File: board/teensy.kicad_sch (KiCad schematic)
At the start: 3 parts, among them J1 RJ45_LED_Shielded, U5 Teensy4.1_DEV-16771

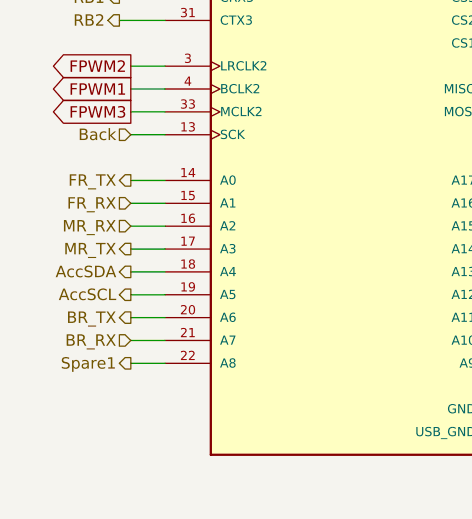
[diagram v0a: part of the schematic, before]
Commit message: Added Temp Sensor
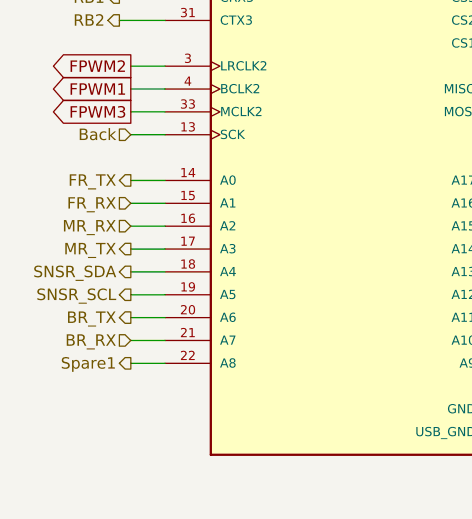
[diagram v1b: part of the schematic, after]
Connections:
- net AccSCL renamed SNSR_SCL
- net AccSDA renamed SNSR_SDA
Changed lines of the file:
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@@
 		)
 	)
-	(hierarchical_label "AccSDA"
+	(hierarchical_label "SNSR_SDA"
 		(shape output)
 		(at 71.12 134.62 180)
@@
 		)
 	)
-	(hierarchical_label "AccSCL"
+	(hierarchical_label "SNSR_SCL"
 		(shape output)
 		(at 71.12 137.16 180)

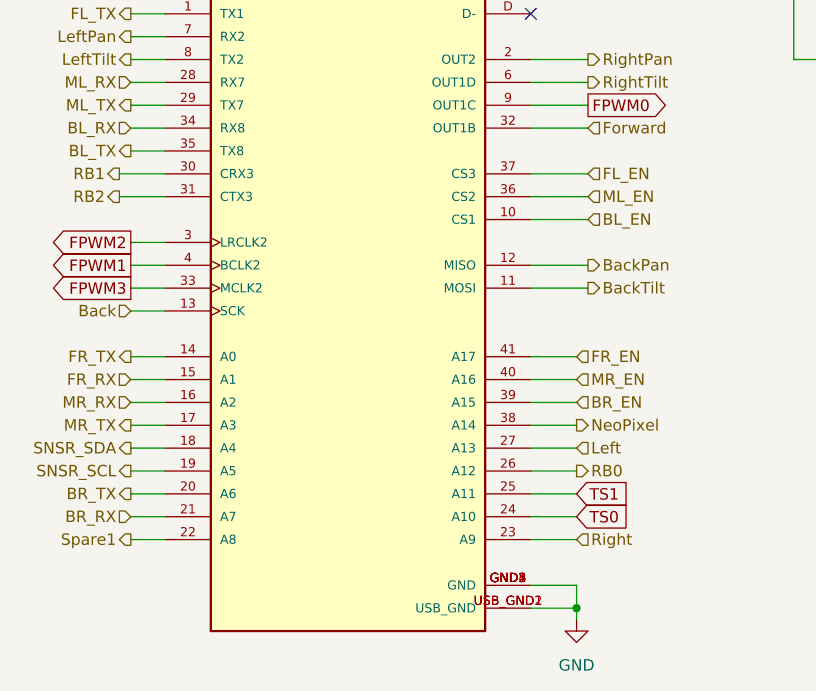
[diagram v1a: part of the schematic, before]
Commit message: Added Rotary Encoder
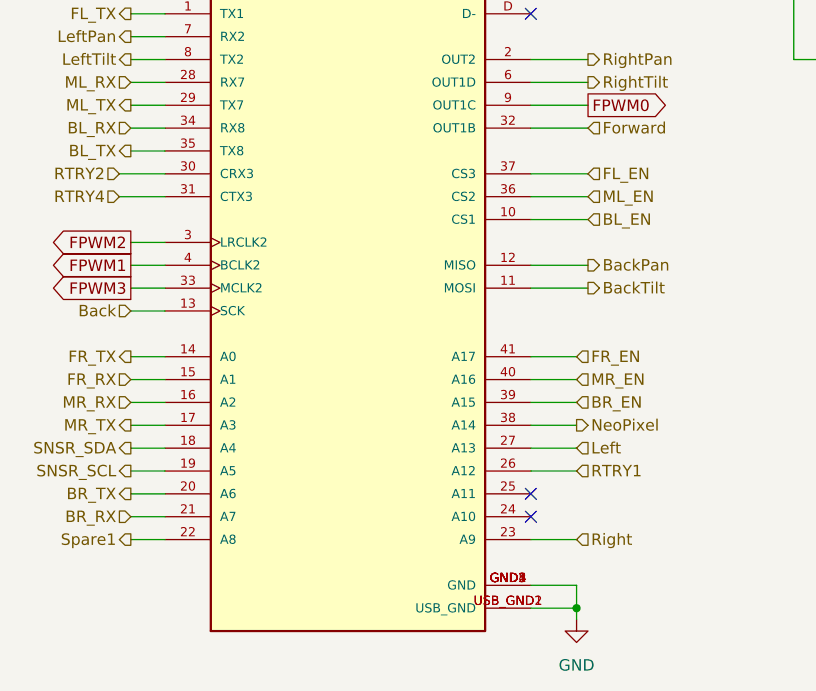
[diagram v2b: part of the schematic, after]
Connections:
- net RB0 renamed RTRY1
- net RB1 renamed RTRY2
- net RB2 renamed RTRY4
- net TS0: no longer names the net of U5.24 (A10)
- net TS1: no longer names the net of U5.25 (A11)
- no-connect marks 9 -> 11

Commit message: Fan, Light, Buck
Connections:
- net FPWM0 is gone; now on net FPWM2: U5.9 (OUT1C)
- net FPWM3 is gone; now on net FPWM1: U5.33 (MCLK2)
- net FPWM1: no longer U5.4 (BCLK2)
- net FPWM2: no longer U5.3 (LRCLK2)
- new net FTACH1: U5.3 (LRCLK2)
- new net FTACH2: U5.4 (BCLK2)

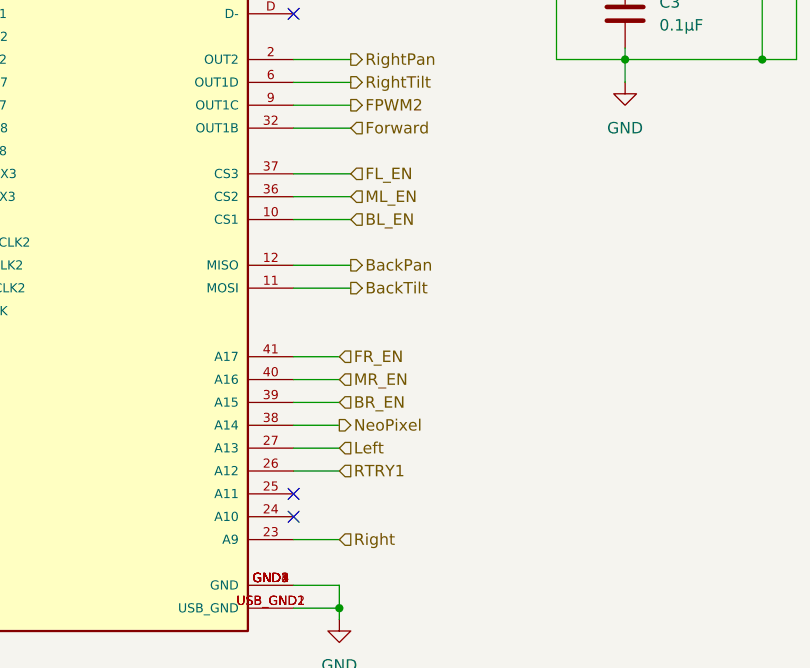
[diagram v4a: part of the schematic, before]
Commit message: routed core board
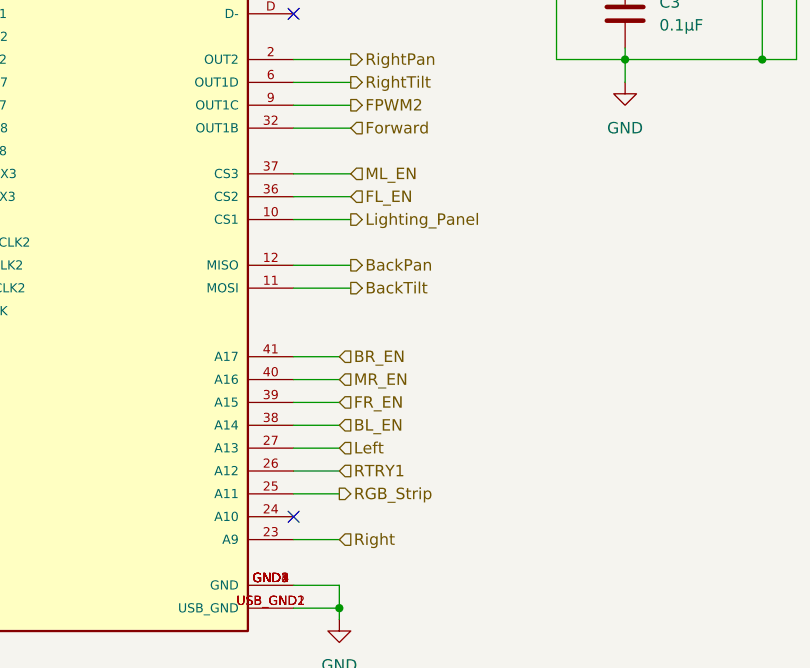
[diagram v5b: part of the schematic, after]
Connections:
- net NeoPixel is gone; now on net BL_EN: U5.38 (A14)
- net BL_EN: no longer U5.10 (CS1)
- net BR_EN: now also U5.41 (A17); no longer U5.39 (A15)
- net FL_EN: now also U5.36 (CS2); no longer U5.37 (CS3)
- net FR_EN: now also U5.39 (A15); no longer U5.41 (A17)
- net ML_EN: now also U5.37 (CS3); no longer U5.36 (CS2)
- net RGB_Strip: now reaches U5.25 (A11)
- new net Lighting_Panel: U5.10 (CS1)
- no-connect marks 11 -> 10

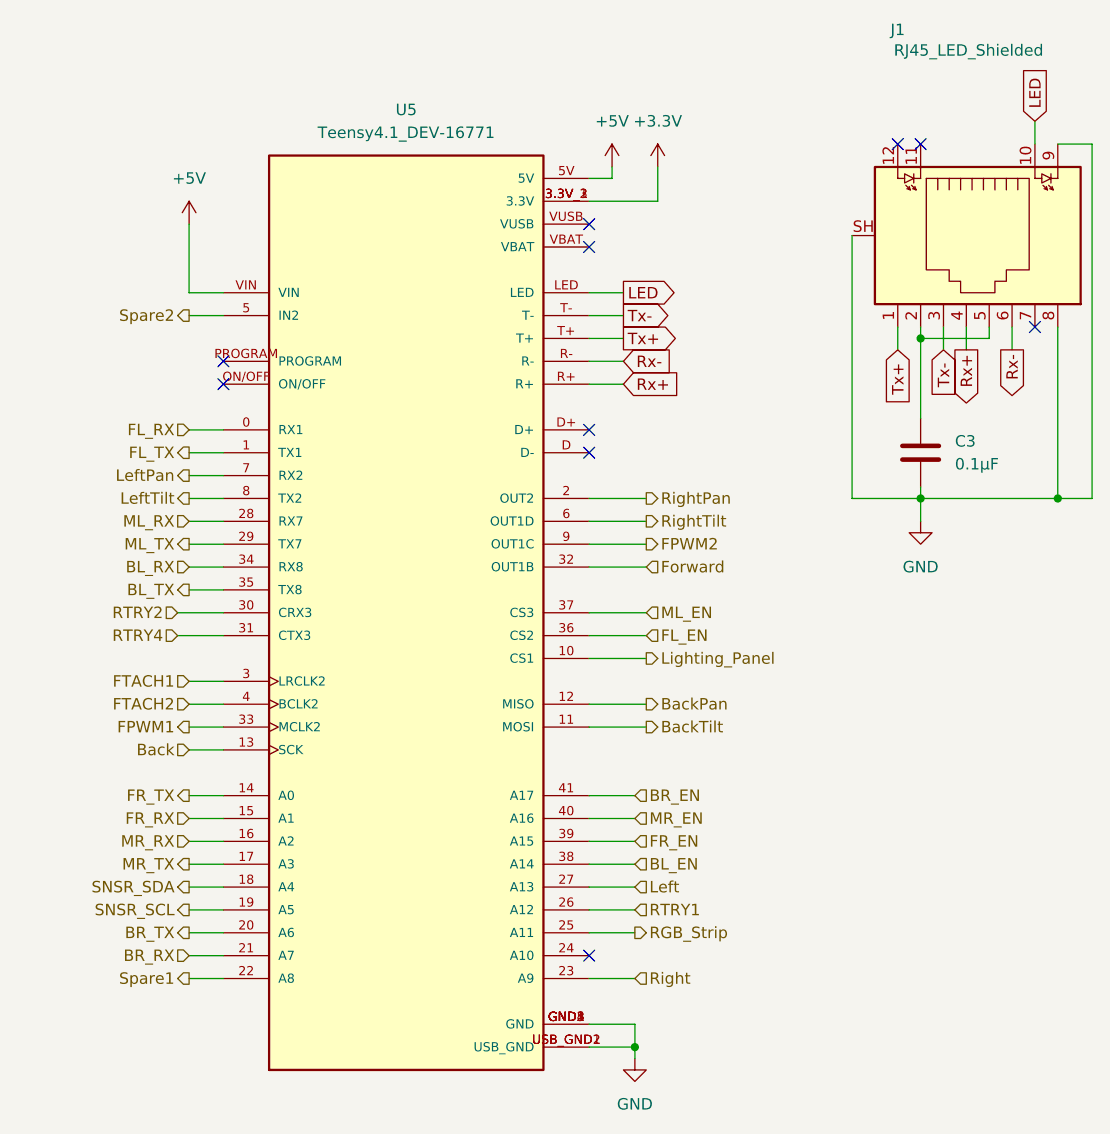
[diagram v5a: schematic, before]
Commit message: Cleaned up traces and silkscreens
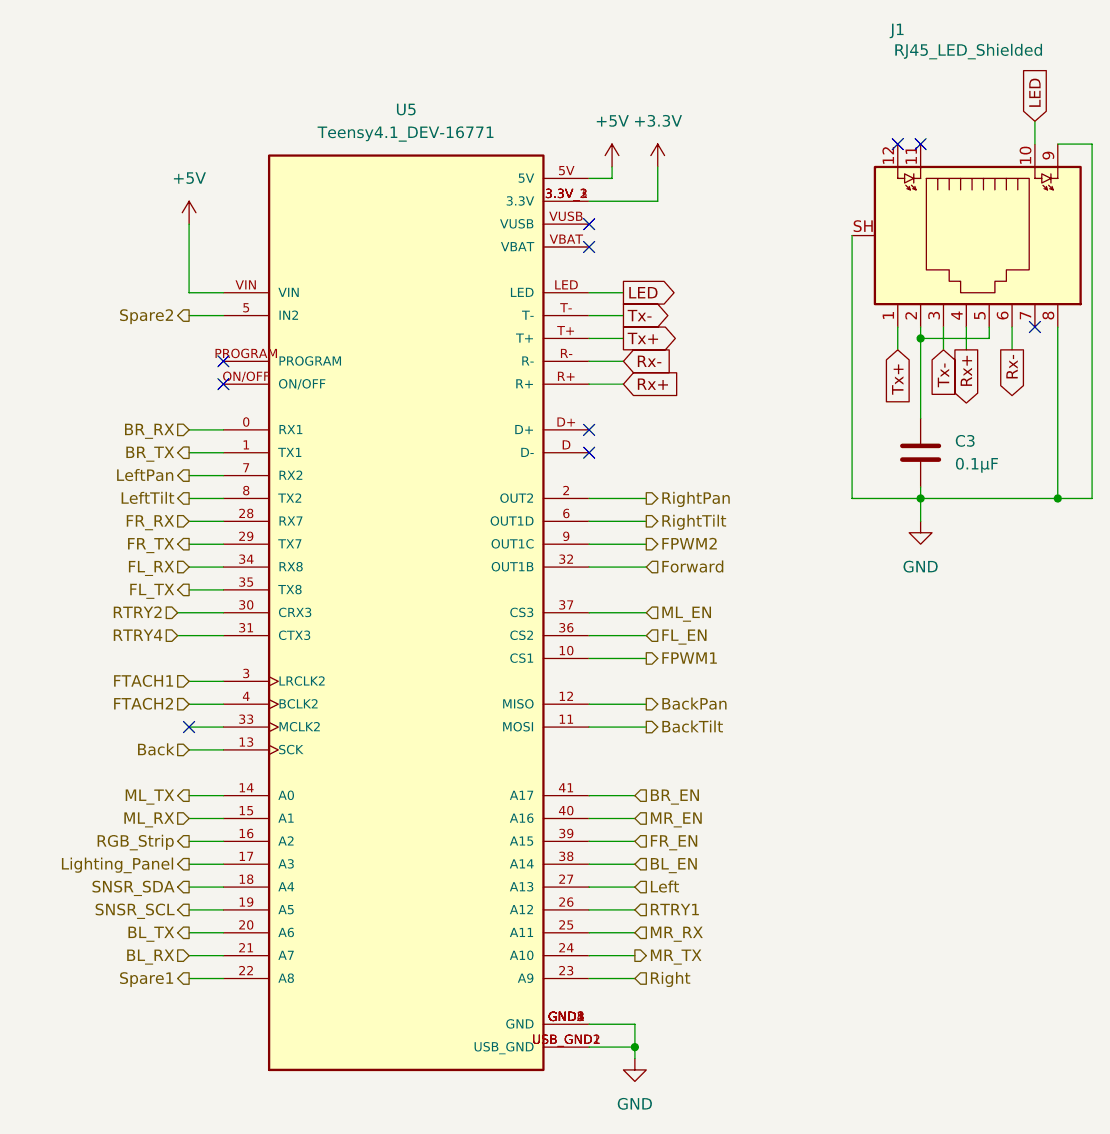
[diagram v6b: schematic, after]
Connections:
- net BL_RX: now also U5.21 (A7); no longer U5.34 (RX8)
- net BL_TX: now also U5.20 (A6); no longer U5.35 (TX8)
- net BR_RX: now also U5.0 (RX1); no longer U5.21 (A7)
- net BR_TX: now also U5.1 (TX1); no longer U5.20 (A6)
- net FL_RX: now also U5.34 (RX8); no longer U5.0 (RX1)
- net FL_TX: now also U5.35 (TX8); no longer U5.1 (TX1)
- net FPWM1: now also U5.10 (CS1); no longer U5.33 (MCLK2)
- net FR_RX: now also U5.28 (RX7); no longer U5.15 (A1)
- net FR_TX: now also U5.29 (TX7); no longer U5.14 (A0)
- net Lighting_Panel: now also U5.17 (A3); no longer U5.10 (CS1)
- net ML_RX: now also U5.15 (A1); no longer U5.28 (RX7)
- net ML_TX: now also U5.14 (A0); no longer U5.29 (TX7)
- net MR_RX: now also U5.25 (A11); no longer U5.16 (A2)
- net MR_TX: now also U5.24 (A10); no longer U5.17 (A3)
- net RGB_Strip: now also U5.16 (A2); no longer U5.25 (A11)

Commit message: rev2 progress
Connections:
- net GStrip: now reaches U5.33 (MCLK2)
- net FPWM2 renamed BStrip
- net FTACH2 renamed RStrip
- no-connect marks 10 -> 9
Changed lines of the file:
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@@
-	)
-	(no_connect
-		(at 71.12 116.84)
 	)
 	(no_connect
@@
 		)
 	)
-	(hierarchical_label "FTACH2"
-		(shape input)
+	(hierarchical_label "RStrip"
+		(shape output)
 		(at 71.12 114.3 180)
 		(effects
@@
 		)
 	)
+	(hierarchical_label "GStrip"
+		(shape output)
+		(at 71.12 116.84 180)
+		(effects
+			(font
+				(size 1.27 1.27)
+			)
+			(justify right)
+		)
+	)
 	(hierarchical_label "FL_RX"
 		(shape input)
@@
 		)
 	)
-	(hierarchical_label "FPWM2"
+	(hierarchical_label "BStrip"
 		(shape output)
 		(at 121.92 96.52 0)
